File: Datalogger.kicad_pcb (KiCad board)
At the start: 2 copper layers, 33 parts, among them J1 From Mains, J2 AVR-ISP-6, J3 USB_B, Q1 BC547, U1 AMS1117-3.3, U2 LM2596T-5, U3 ATmega2560-16A, Y1 16MHz

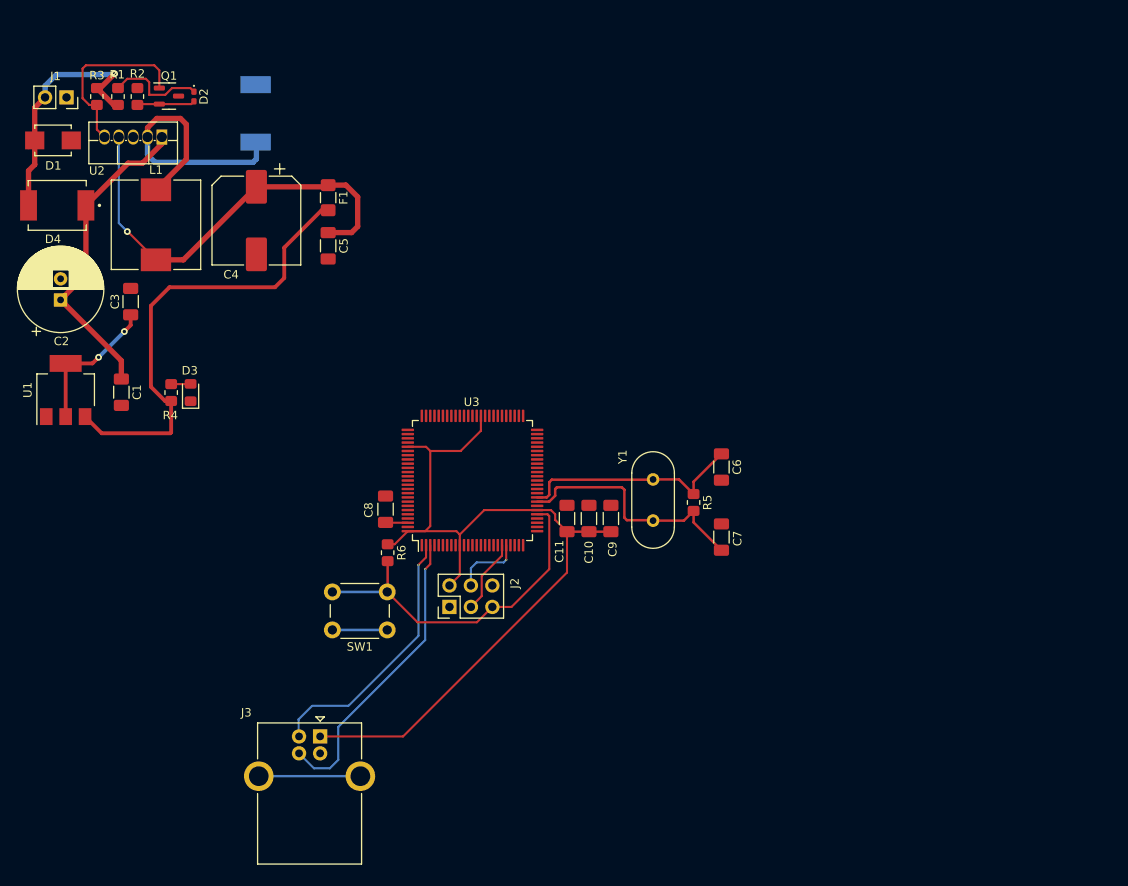
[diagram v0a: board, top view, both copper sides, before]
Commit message: "Resolved the issue of SS34 diode footprint. Problem was the pin on the downloaded footprint were not numbered
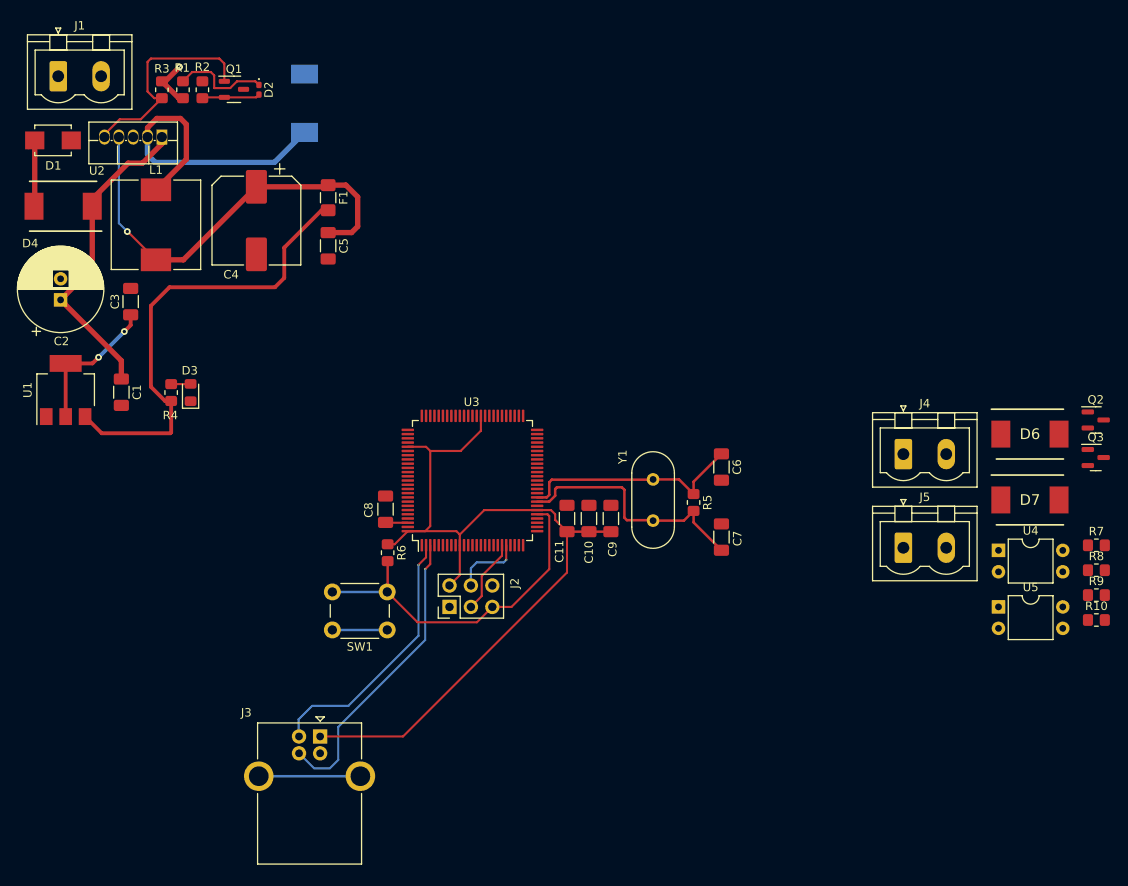
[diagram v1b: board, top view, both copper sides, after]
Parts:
- added D6: ~, KiCad:DIOM8059X256N, F.Cu at (200.8, 87.0)
- added D7: ~, KiCad:DIOM8059X256N, F.Cu at (200.8, 94.8)
- added J4: Screw, Connector_Phoenix_MSTB:PhoenixContact_MSTBVA_2,5_2-G-5,08_1x02_P5.08mm_Vertical, F.Cu at (185.9, 89.4)
- added J5: Screw, Connector_Phoenix_MSTB:PhoenixContact_MSTBVA_2,5_2-G-5,08_1x02_P5.08mm_Vertical, F.Cu at (185.9, 100.5)
- added Q2: BC847, Package_TO_SOT_SMD:SOT-23, F.Cu at (208.6, 85.3)
- added Q3: BC847, Package_TO_SOT_SMD:SOT-23, F.Cu at (208.6, 89.8)
- added R10: 1k, Resistor_SMD:R_0805_2012Metric_Pad1.20x1.40mm_HandSolder, F.Cu at (208.7, 109.0)
- added R7: 1k, Resistor_SMD:R_0805_2012Metric_Pad1.20x1.40mm_HandSolder, F.Cu at (208.7, 100.2)
- added R8: 1k, Resistor_SMD:R_0805_2012Metric_Pad1.20x1.40mm_HandSolder, F.Cu at (208.7, 103.1)
- added R9: 1k, Resistor_SMD:R_0805_2012Metric_Pad1.20x1.40mm_HandSolder, F.Cu at (208.7, 106.1)
- added U4: PC817, Package_DIP:DIP-4_W7.62mm, F.Cu at (197.1, 100.8)
- added U5: PC817, Package_DIP:DIP-4_W7.62mm, F.Cu at (197.1, 107.5)
- D4, D5: footprint SS34:DIO_SS34 -> KiCad:DIOM8059X256N
- J1: footprint Connector_PinSocket_2.54mm:PinSocket_1x02_P2.54mm_Vertical -> Connector_Phoenix_MSTB:PhoenixContact_MSTBVA_2,5_2-G-5,08_1x02_P5.08mm_Vertical
- moved D2 7.74 mm to (109.5, 46.2)
- moved R1 7.74 mm to (100.5, 46.2)
- moved R2 7.74 mm to (102.8, 46.2)
- moved R3 7.74 mm to (98.0, 46.2)
- moved Q1 7.74 mm to (106.5, 46.1)
- moved D5 5.92 mm to (114.9, 47.8)
- moved J1 2.69 mm to (85.7, 44.6), turned to 0 degrees
- moved D4 0.71 mm to (86.3, 60.0)
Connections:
- U3 pad 53: unconnected-(U3-PC0-Pad53) -> /ATMEGA2560/Relay_1
- U3 pad 54: unconnected-(U3-PC1-Pad54) -> /ATMEGA2560/Relay_2
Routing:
- net +12V: track 31.0 -> 15.1 mm
- net Net-(D5-K): track 33.3 -> 38.2 mm
- net ON/OFF: track 21.3 -> 26.0 mm

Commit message: Added DC motor driver
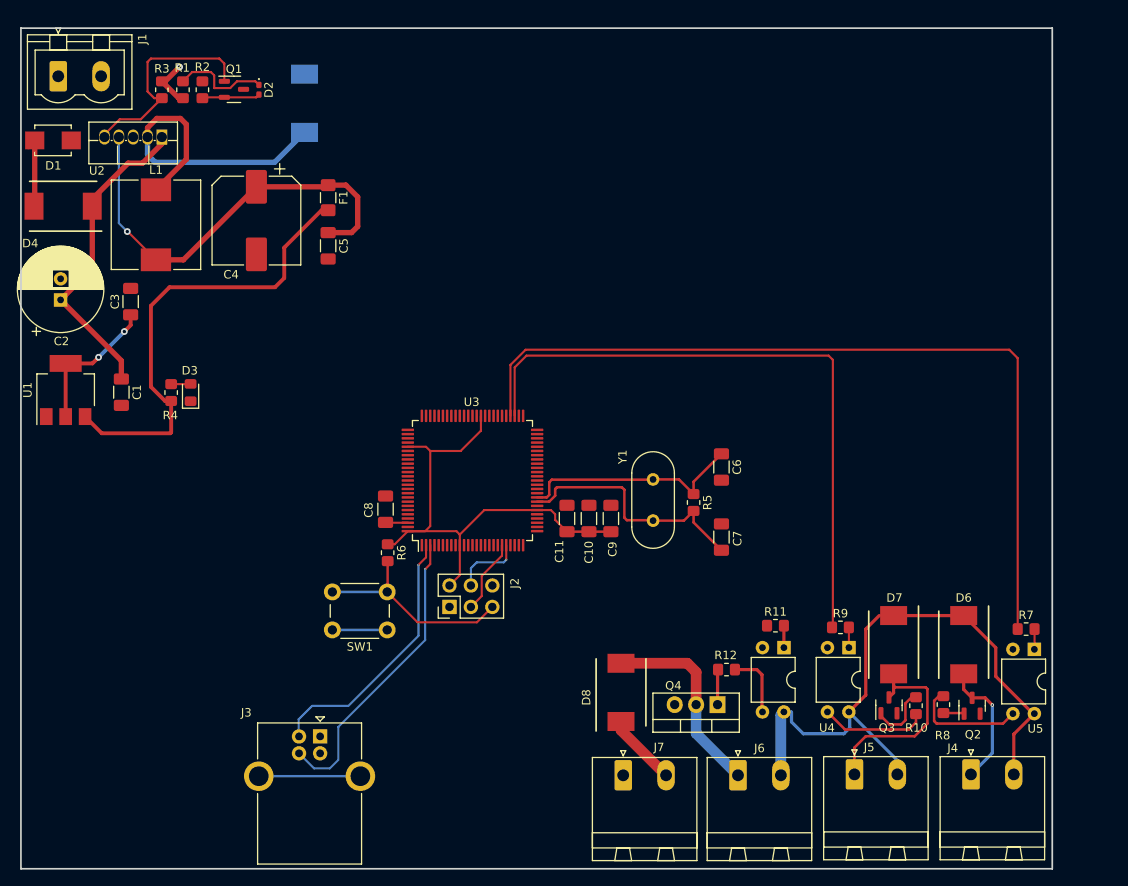
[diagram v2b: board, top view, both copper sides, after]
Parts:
- added D8: ~, KiCad:DIOM8059X256N, F.Cu at (152.4, 117.6)
- added J6: Screw, Connector_Phoenix_MSTB:PhoenixContact_MSTBA_2,5_2-G-5,08_1x02_P5.08mm_Horizontal, F.Cu at (166.3, 127.4)
- added J7: Screw, Connector_Phoenix_MSTB:PhoenixContact_MSTBA_2,5_2-G-5,08_1x02_P5.08mm_Horizontal, F.Cu at (152.7, 127.4)
- added Q4: TIP127, Package_TO_SOT_THT:TO-220-3_Vertical, F.Cu at (163.8, 119.1)
- added R11: 1k, Resistor_SMD:R_0805_2012Metric_Pad1.20x1.40mm_HandSolder, F.Cu at (170.7, 109.7)
- added R12: 1k, Resistor_SMD:R_0805_2012Metric_Pad1.20x1.40mm_HandSolder, F.Cu at (164.9, 114.9)
- added U6: PC817, Package_DIP:DIP-4_W7.62mm, F.Cu at (171.7, 112.3)
- J4, J5: footprint Connector_Phoenix_MSTB:PhoenixContact_MSTBVA_2,5_2-G-5,08_1x02_P5.08mm_Vertical -> Connector_Phoenix_MSTB:PhoenixContact_MSTBA_2,5_2-G-5,08_1x02_P5.08mm_Horizontal
- moved J4 38.8 mm to (193.9, 127.3)
- moved Q3 38.2 mm to (184.2, 119.1), turned to 90 degrees
- moved Q2 36.9 mm to (194.0, 119.2), turned to 90 degrees
- moved R9 30.6 mm to (178.4, 109.9)
- moved J5 27.5 mm to (180.1, 127.3)
- moved D6 26.2 mm to (193.0, 112.0), turned to -90 degrees
- moved R8 24.1 mm to (190.6, 119.0), turned to -90 degrees
- moved R10 23.7 mm to (187.3, 119.2), turned to 90 degrees
- moved D7 23.6 mm to (184.7, 112.0), turned to -90 degrees
- moved U4 21.1 mm to (179.4, 112.3), turned to -90 degrees
- moved R7 13.0 mm to (200.4, 110.1)
- moved U5 6.58 mm to (201.4, 112.5), turned to -90 degrees
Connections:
- R7 pad 1: /ATMEGA2560/Relay_1 -> /ATMEGA2560/Relay_2
- R9 pad 1: /ATMEGA2560/Relay_2 -> /ATMEGA2560/Relay_1
- U3 pad 15: unconnected-(U3-PH3-Pad15) -> /ATMEGA2560/MTR_CTRL
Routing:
- net /ATMEGA2560/Relay_2: track 0.00 -> 99.4 mm
- net +12VA: track 0.00 -> 84.7 mm
- net /ATMEGA2560/Relay_1: track 0.00 -> 76.0 mm
- net +5V: track 157.3 -> 115.2 mm
- net Net-(D7-A): track 0.00 -> 24.3 mm
- net Net-(D8-A): track 0.00 -> 23.6 mm
- net RST: track 41.3 -> 24.9 mm
- net Net-(D6-A): track 0.00 -> 15.3 mm, vias 0 -> 1
- net Net-(R8-Pad1): track 0.00 -> 13.7 mm
- net Net-(R10-Pad1): track 0.00 -> 12.7 mm
- net Net-(R12-Pad1): track 0.00 -> 7.89 mm
- net Net-(Q3-B): track 0.00 -> 7.40 mm
- net Net-(Q4-B): track 0.00 -> 4.18 mm
- net Net-(R11-Pad2): track 0.00 -> 2.60 mm
- net Net-(Q2-B): track 0.00 -> 2.48 mm
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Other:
- board outline added: 122.2 x 99.6 mm

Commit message: Designed circuit for reading digital input. CHY74 (4 channel optocoupler) used
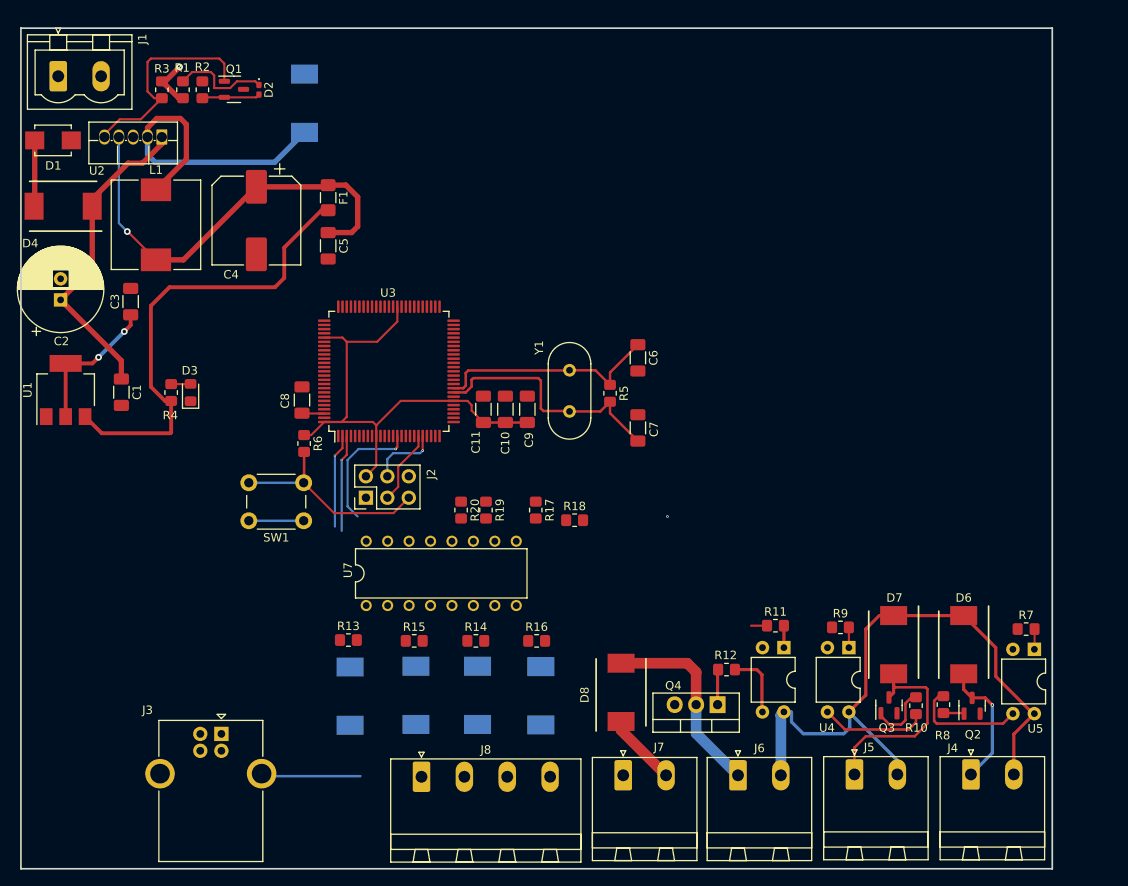
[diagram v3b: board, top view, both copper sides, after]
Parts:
- added D10: ~, KiCad:DIOM8059X256N, B.Cu at (135.4, 118.0)
- added D11: ~, KiCad:DIOM8059X256N, B.Cu at (120.3, 118.0)
- added D12: ~, KiCad:DIOM8059X256N, B.Cu at (142.9, 118.0)
- added D9: ~, KiCad:DIOM8059X256N, B.Cu at (128.1, 118.0)
- added J8: Conn_01x04_Socket, Connector_Phoenix_MSTB:PhoenixContact_MSTBA_2,5_4-G-5,08_1x04_P5.08mm_Horizontal, F.Cu at (128.8, 127.6)
- added R13: 1k, Resistor_SMD:R_0805_2012Metric_Pad1.20x1.40mm_HandSolder, F.Cu at (120.1, 111.4)
- added R14: 1k, Resistor_SMD:R_0805_2012Metric_Pad1.20x1.40mm_HandSolder, F.Cu at (135.2, 111.5)
- added R15: 1k, Resistor_SMD:R_0805_2012Metric_Pad1.20x1.40mm_HandSolder, F.Cu at (127.9, 111.5)
- added R16: 1k, Resistor_SMD:R_0805_2012Metric_Pad1.20x1.40mm_HandSolder, F.Cu at (142.4, 111.5)
- added R17: 1k, Resistor_SMD:R_0805_2012Metric_Pad1.20x1.40mm_HandSolder, F.Cu at (142.3, 96.0)
- added R18: 1k, Resistor_SMD:R_0805_2012Metric_Pad1.20x1.40mm_HandSolder, F.Cu at (146.9, 97.2)
- added R19: 1k, Resistor_SMD:R_0805_2012Metric_Pad1.20x1.40mm_HandSolder, F.Cu at (136.4, 96.0)
- added R20: 1k, Resistor_SMD:R_0805_2012Metric_Pad1.20x1.40mm_HandSolder, F.Cu at (133.4, 96.0)
- added U7: CNY74-4H, CNY74-4H:DIL16, F.Cu at (131.1, 103.5)
- moved C10 16.3 mm to (138.7, 84.1)
- moved C11 16.3 mm to (136.1, 84.1)
- moved C6 16.3 mm to (154.4, 78.0)
- moved C7 16.3 mm to (154.4, 86.3)
- moved C8 16.3 mm to (114.6, 83.0)
- moved R5 16.3 mm to (151.1, 82.2)
- moved R6 16.3 mm to (114.8, 88.1)
- moved SW1 16.3 mm to (114.8, 97.3)
- moved U3 16.3 mm to (124.9, 79.6)
- moved J2 16.3 mm to (122.2, 94.5)
- moved C9 16.3 mm to (141.3, 84.1)
- moved Y1 16.3 mm to (146.3, 84.3)
- moved J3 11.7 mm to (105.0, 122.5)
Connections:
- U3 pad 66: unconnected-(U3-PJ3-Pad66) -> /ATMEGA2560/DIN1
- U3 pad 67: unconnected-(U3-PJ4-Pad67) -> /ATMEGA2560/DIN2
- U3 pad 68: unconnected-(U3-PJ5-Pad68) -> /ATMEGA2560/DIN3
- U3 pad 69: unconnected-(U3-PJ6-Pad69) -> /ATMEGA2560/DIN4
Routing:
- net /ATMEGA2560/Relay_2: track 99.4 -> 0.00 mm
- net /ATMEGA2560/Relay_1: track 76.0 -> 0.14 mm
- net PROG_TX0: track 35.8 -> 11.5 mm
- net PROG_RX0: track 31.5 -> 11.1 mm
- net /ATMEGA2560/MTR_CTRL: track 0.00 -> 17.0 mm, vias 0 -> 2

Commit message: pictures
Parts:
- D10, D11, D12, D9: moved to F.Cu
- moved J7 89.9 mm to (198.9, 50.3), turned to 180 degrees
- moved J4 85.0 mm to (157.7, 50.4), turned to 180 degrees
- moved J6 79.4 mm to (185.3, 50.3), turned to 180 degrees
- moved J5 77.4 mm to (171.5, 50.4), turned to 180 degrees
- moved D8 74.1 mm to (199.1, 60.1), turned to -90 degrees
- moved Q2 70.8 mm to (157.5, 58.5), turned to -90 degrees
- moved U5 69.7 mm to (150.2, 65.2), turned to 90 degrees
- moved R8 67.3 mm to (160.9, 58.7), turned to 90 degrees
- moved R7 65.0 mm to (151.1, 67.6), turned to 180 degrees
- moved Q4 64.9 mm to (187.7, 58.7), turned to 0 degrees
- moved R10 64.9 mm to (164.2, 58.5), turned to -90 degrees
- moved Q3 62.8 mm to (167.4, 58.6), turned to -90 degrees
- moved D6 57.6 mm to (158.5, 65.8), turned to 90 degrees
- moved R12 56.4 mm to (186.6, 62.8), turned to 0 degrees
- moved D7 49.5 mm to (166.8, 65.8), turned to 90 degrees
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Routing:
- net Net-(R13-Pad2): track 0.00 -> 21.8 mm, vias 0 -> 1
- net Net-(R16-Pad2): track 0.00 -> 21.6 mm, vias 0 -> 1
- net unconnected-(J3-Shield-Pad5): track 12.0 -> 0.00 mm
- net Net-(D9-A): track 0.00 -> 9.67 mm
- net Net-(D12-A): track 0.00 -> 9.04 mm
- net Net-(R15-Pad2): track 0.00 -> 7.79 mm, vias 0 -> 1
- net Net-(R14-Pad2): track 0.00 -> 7.78 mm
- net Net-(D10-A): track 0.00 -> 7.33 mm
- net Net-(D11-A): track 0.00 -> 6.55 mm
- net Net-(D11-K): track 0.00 -> 3.35 mm
- net Net-(D9-K): track 0.00 -> 3.25 mm
- net Net-(D10-K): track 0.00 -> 3.25 mm
- net Net-(D12-K): track 0.00 -> 3.05 mm
- net /Digital Pin/DIN2: track 0.00 -> 2.92 mm
- net /Digital Pin/DIN1: track 0.00 -> 2.91 mm
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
